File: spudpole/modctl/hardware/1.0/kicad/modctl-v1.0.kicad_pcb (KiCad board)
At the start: 2 copper layers, 75 x 75 mm, 35 parts, among them J1 SWITCH INPUTS ->, J2 OUTPUTS, J3 M12-5PIN, SW1 PRG_SPUD0, SW2 PRG_SPUD1, SW3 INSTANCE, U1 POWER, U10 MCP2551-I-P, U2 POLE0_UP, U3 CNY74-4H, U4 POLE0_DN, U5 POLE1_UP, U6 POLE1_DN, U8 Teensy_3.2, U9 TEC2-2411WI

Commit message: Many tweaks, plus a latex pretty print
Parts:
- added D5: LED_Small, LED_THT:LED_D3.0mm, F.Cu at (51.4, 82.5)
- added R5: 270R, Resistor_THT:R_Axial_DIN0204_L3.6mm_D1.6mm_P5.08mm_Horizontal, F.Cu at (52.7, 87.6)
- J1: value SWITCH INPUTS -> -> SWITCH INPUTS
- J2: value OUTPUTS -> Screw_Terminal_01x10
- renumbered R5 to R6, R6 to R7, R7 to R8, U8 to U7, U9 to U8, U10 to U9
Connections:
- U7 pad 3: (no net) -> Net-(D5-Pad1)
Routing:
- net Net-(D5-Pad1): track 0.00 -> 15.7 mm
- net Net-(D5-Pad2): track 0.00 -> 3.07 mm

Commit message: Utility and config changes
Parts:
- removed the D2 at (-5.71, 68.6)
- added R6: 270R, Resistor_THT:R_Axial_DIN0204_L3.6mm_D1.6mm_P5.08mm_Horizontal, F.Cu at (48.3, 55.2)
- added R7: 270R, Resistor_THT:R_Axial_DIN0204_L3.6mm_D1.6mm_P5.08mm_Horizontal, F.Cu at (48.3, 64.1)
- D1: value 4 x 1N4007 -> 1N4007
- D2: renamed from D5; value LED_Small -> PWR
- D3: value 1N4007 -> UP; footprint Diode_THT:D_DO-35_SOD27_P2.54mm_Vertical_AnodeUp -> LED_THT:LED_D3.0mm
- D4: value 1N4007 -> DN; footprint Diode_THT:D_DO-35_SOD27_P2.54mm_Vertical_AnodeUp -> LED_THT:LED_D3.0mm
- J2: value Screw_Terminal_01x10 -> RELAY OUTPUTS
- R1: value 4 x 1K4, 1W -> 1K4
- R2, R3, R4: value 1K4, 1W -> 1K4
- SW1: value PRG_SPUD0 -> PRGW0
- SW2: value PRG_SPUD1 -> PRGW1
- U1: value POWER -> 291-9669; footprint pdjr:SPNO-SIL -> pdjr:291-9669
- U2: value POLE0_UP -> 291-9669; footprint pdjr:SPNO-SIL -> pdjr:291-9669
- U4: value POLE0_DN -> 291-9669; footprint pdjr:SPNO-SIL -> pdjr:291-9669
- U5: value POLE1_UP -> 291-9669; footprint pdjr:SPNO-SIL -> pdjr:291-9669
- U6: value POLE1_DN -> 291-9669; footprint pdjr:SPNO-SIL -> pdjr:291-9669
- moved D3 57.1 mm to (52.1, 54.0), turned to 270 degrees
- moved D4 48.3 mm to (52.1, 60.3), turned to 270 degrees
- moved D1 26.3 mm to (11.4, 77.5), turned to 90 degrees
- moved C1 16.9 mm to (10.2, 69.2), turned to 180 degrees
- moved D2 15.9 mm to (52.1, 66.7)
- moved R5 15.3 mm to (52.1, 72.4), turned to 270 degrees
- moved SW3 10.3 mm to (34.9, 52.1)
- moved U7 5.71 mm to (23.5, 68.6)
- moved SW1 4.96 mm to (23.5, 45.1), turned to 90 degrees
- moved SW2 4.26 mm to (34.9, 45.1), turned to 90 degrees
- turned U1 to 270 degrees
- turned U2 to 270 degrees
- turned U4 to 270 degrees
- turned U5 to 270 degrees
- turned U6 to 270 degrees
- renumbered R8 to R10, R6 to R8, R7 to R9
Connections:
- D2 pad 1: Net-(D5-Pad1) -> GND
- D2 pad 2: Net-(D5-Pad2) -> Net-(D2-Pad2)
- D3 pad 1: Net-(D3-Pad1) -> GND
- D3 pad 2: Net-(D1-Pad2) -> Net-(D3-Pad2)
- D4 pad 1: Net-(D4-Pad1) -> GND
- D4 pad 2: Net-(D1-Pad2) -> Net-(D4-Pad2)
- J1 pad 5: Net-(D1-Pad2) -> Net-(D1-Pad1)
- R1 pad 2: Net-(D1-Pad1) -> Net-(R1-Pad2)
- R3 pad 2: Net-(D3-Pad1) -> Net-(R3-Pad2)
- R4 pad 2: Net-(D4-Pad1) -> Net-(R4-Pad2)
- R5 pad 1: Net-(D5-Pad2) -> Net-(R5-Pad1)
- R5 pad 2: Net-(C1-Pad1) -> Net-(D2-Pad2)
- SW1 pad 1: Net-(SW1-Pad1) -> GND
- SW1 pad 2: GND -> Net-(SW1-Pad2)
- SW2 pad 1: GND -> Net-(SW2-Pad1)
- SW2 pad 2: Net-(SW2-Pad2) -> GND
- U1 pad 1: Net-(J2-Pad2) -> Net-(J2-Pad1)
- U1 pad 3: GND -> Net-(U1-Pad3)
- U1 pad 5: Net-(U1-Pad5) -> GND
- U1 pad 7: Net-(J2-Pad1) -> Net-(J2-Pad2)
- U2 pad 1: Net-(J2-Pad4) -> Net-(J2-Pad3)
- U2 pad 3: GND -> Net-(U2-Pad3)
- U2 pad 5: Net-(U2-Pad5) -> GND
- U2 pad 7: Net-(J2-Pad3) -> Net-(J2-Pad4)
- U3 pad 1: Net-(D1-Pad1) -> Net-(R1-Pad2)
- U3 pad 5: Net-(D3-Pad1) -> Net-(R3-Pad2)
- U3 pad 8: Net-(D4-Pad1) -> Net-(R4-Pad2)
- U4 pad 1: Net-(J2-Pad6) -> Net-(J2-Pad5)
- U4 pad 3: GND -> Net-(U4-Pad3)
- U4 pad 5: Net-(U4-Pad5) -> GND
- U4 pad 7: Net-(J2-Pad5) -> Net-(J2-Pad6)
- U5 pad 1: Net-(J2-Pad8) -> Net-(J2-Pad7)
- U5 pad 3: GND -> Net-(U5-Pad3)
- U5 pad 5: Net-(U5-Pad5) -> GND
- U5 pad 7: Net-(J2-Pad7) -> Net-(J2-Pad8)
- U6 pad 1: Net-(J2-Pad10) -> Net-(J2-Pad9)
- U6 pad 3: GND -> Net-(U6-Pad3)
- U6 pad 5: Net-(U6-Pad5) -> GND
- U6 pad 7: Net-(J2-Pad9) -> Net-(J2-Pad10)
- U7 pad 19: (no net) -> Net-(U6-Pad3)
- U7 pad 2: Net-(SW2-Pad2) -> Net-(R7-Pad1)
- U7 pad 20: Net-(U6-Pad5) -> Net-(U5-Pad3)
- U7 pad 21: Net-(U5-Pad5) -> Net-(U4-Pad3)
- U7 pad 22: Net-(U4-Pad5) -> Net-(U2-Pad3)
- U7 pad 23: Net-(U2-Pad5) -> Net-(U1-Pad3)
- U7 pad 24: Net-(U1-Pad5) -> Net-(SW1-Pad2)
- U7 pad 25: Net-(SW1-Pad1) -> Net-(SW2-Pad1)
- U7 pad 3: Net-(D5-Pad1) -> Net-(R6-Pad1)
- U7 pad 4: (no net) -> Net-(R5-Pad1)
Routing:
- net Net-(U1-Pad5): track 65.4 -> 0.00 mm
- net Net-(U2-Pad5): track 58.2 -> 0.00 mm
- net Net-(U1-Pad3): track 0.00 -> 58.2 mm
- net Net-(U4-Pad5): track 51.1 -> 0.00 mm
- net Net-(U2-Pad3): track 0.00 -> 51.1 mm
- net Net-(SW2-Pad1): track 0.00 -> 48.8 mm
- net Net-(U5-Pad5): track 44.0 -> 0.00 mm
- net Net-(U4-Pad3): track 0.00 -> 42.8 mm
- net Net-(R6-Pad1): track 0.00 -> 40.1 mm
- net Net-(SW1-Pad2): track 0.00 -> 39.6 mm
- net Net-(U6-Pad5): track 36.8 -> 0.00 mm
- net Net-(SW2-Pad2): track 36.5 -> 0.00 mm
- net Net-(U5-Pad3): track 0.00 -> 35.3 mm
- net Net-(R7-Pad1): track 0.00 -> 32.2 mm
- net Net-(SW1-Pad1): track 31.4 -> 0.00 mm
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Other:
- board text added: "MODCTL"
- board text added: "MODCTL 1.0"
- board text added: "NMEA 2000 Windlass Control Interface Module"
- board text added: "PDJR.EU"
- board text added: "PWR/RX"
- board text added: "SPUD/W0"
- board text added: "SPUD/W1"

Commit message: testing...
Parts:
- R8: footprint Resistor_THT:R_Axial_DIN0204_L3.6mm_D1.6mm_P2.54mm_Vertical -> Resistor_THT:R_Axial_DIN0204_L3.6mm_D1.6mm_P5.08mm_Horizontal
- SW3: footprint Button_Switch_THT:SW_DIP_SPSTx08_Slide_6.7x21.88mm_W7.62mm_P2.54mm_LowProfile -> Package_DIP:DIP-14_W7.62mm_Socket
- U1: value 291-9669 -> POWER
- U2: value 291-9669 -> W0UP
- U4: value 291-9669 -> W0DN
- U5: value 291-9669 -> W1UP
- U6: value 291-9669 -> W1DN
- moved R8 7.24 mm to (19.1, 36.2), turned to 0 degrees
- moved R10 1.91 mm to (19.1, 31.1)
- moved R9 1.91 mm to (24.1, 33.7)
- moved J3 1.27 mm to (29.2, 22.2)
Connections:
- SW3 pad 8: Net-(SW3-Pad8) -> GND
- U7 pad 15: Net-(U3-Pad15) -> (no net)
- U7 pad 16: Net-(U3-Pad14) -> Net-(U3-Pad15)
- U7 pad 17: Net-(U3-Pad11) -> Net-(U3-Pad14)
- U7 pad 18: Net-(U3-Pad10) -> Net-(U3-Pad11)
- U7 pad 19: Net-(U6-Pad3) -> Net-(U3-Pad10)
- U7 pad 2: Net-(R7-Pad1) -> Net-(SW2-Pad1)
- U7 pad 20: Net-(U5-Pad3) -> Net-(U6-Pad3)
- U7 pad 21: Net-(U4-Pad3) -> Net-(U5-Pad3)
- U7 pad 22: Net-(U2-Pad3) -> Net-(U4-Pad3)
- U7 pad 23: Net-(U1-Pad3) -> Net-(U2-Pad3)
- U7 pad 24: Net-(SW1-Pad2) -> Net-(U1-Pad3)
- U7 pad 25: Net-(SW2-Pad1) -> Net-(SW1-Pad2)
- U7 pad 3: Net-(R6-Pad1) -> Net-(R7-Pad1)
- U7 pad 4: Net-(R5-Pad1) -> Net-(R6-Pad1)
- U7 pad 7: Net-(SW3-Pad8) -> Net-(R5-Pad1)
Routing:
- net Net-(R7-Pad1): track 32.2 -> 69.0 mm
- net Net-(R8-Pad2): track 17.5 -> 3.18 mm
- net Net-(R6-Pad1): track 40.1 -> 51.3 mm
- net Net-(U1-Pad3): track 58.2 -> 64.1 mm
- net Net-(U5-Pad3): track 35.3 -> 41.0 mm
- net Net-(U4-Pad3): track 42.8 -> 47.8 mm
- net Net-(U2-Pad3): track 51.1 -> 55.7 mm
- net Net-(C3-Pad1): track 13.2 -> 17.5 mm
- net Net-(SW3-Pad8): track 3.81 -> 0.00 mm
- net Net-(R5-Pad1): track 25.3 -> 22.0 mm
- net Net-(SW2-Pad1): track 48.8 -> 45.7 mm
- net Net-(U6-Pad3): track 29.3 -> 32.0 mm
- net Net-(SW1-Pad2): track 39.6 -> 42.1 mm
- net Net-(U3-Pad10): track 16.4 -> 18.7 mm
- net Net-(J3-Pad4): track 22.8 -> 20.8 mm
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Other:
- board text removed: "128"

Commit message: Refactor
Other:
- board text added: "W0"
- board text added: "W1"
- board text removed: "SPUD/W0"
- board text removed: "SPUD/W1"

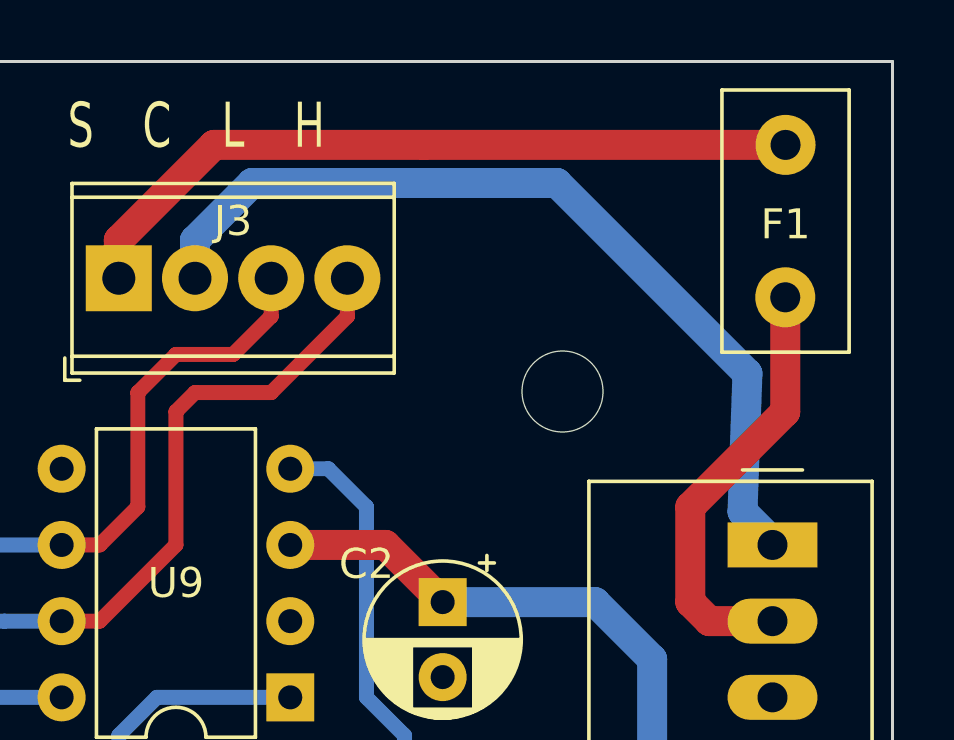
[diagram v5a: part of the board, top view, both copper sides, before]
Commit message: Grounded NMEA C connection
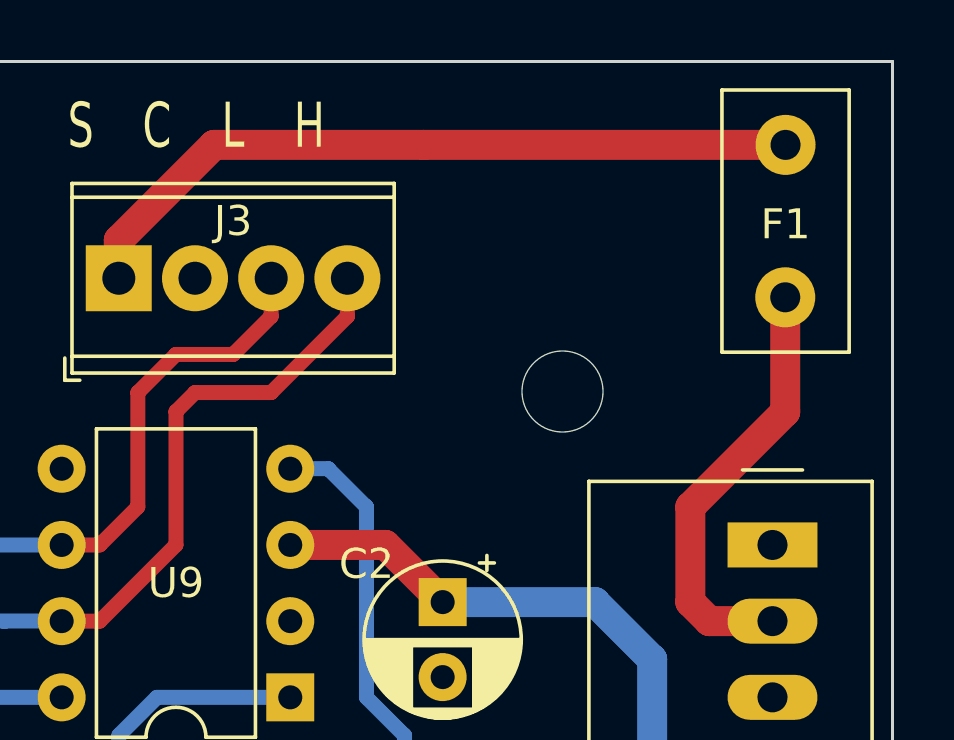
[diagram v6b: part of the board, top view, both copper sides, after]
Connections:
- J3 pad 2: Net-(J3-Pad2) -> GND
- U8 pad 1: Net-(J3-Pad2) -> GND
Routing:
- net Net-(J3-Pad2): track 29.2 -> 0.00 mm

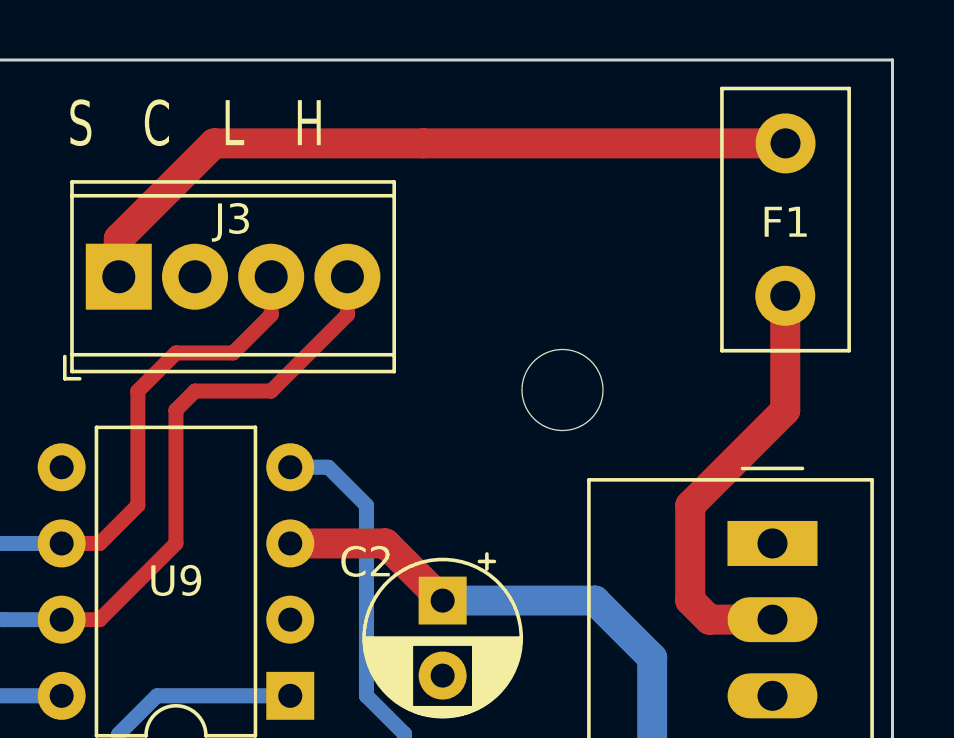
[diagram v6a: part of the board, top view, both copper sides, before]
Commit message: New print script
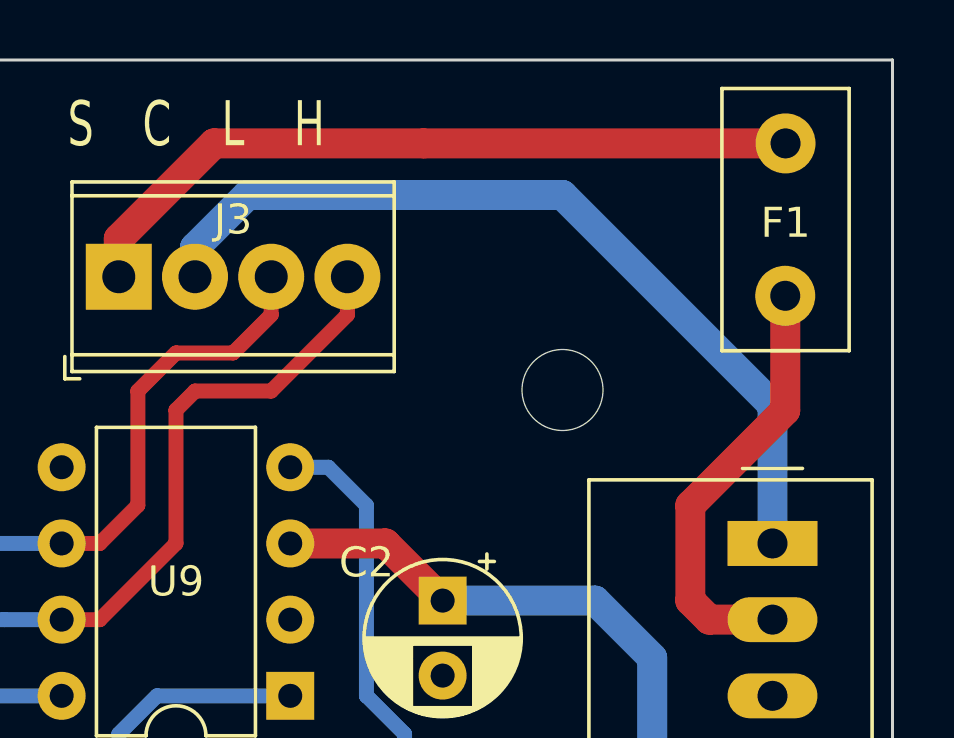
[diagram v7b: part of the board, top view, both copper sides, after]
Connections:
- J3 pad 2: GND -> Net-(J3-Pad2)
- U8 pad 1: GND -> Net-(J3-Pad2)
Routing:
- net Net-(J3-Pad2): track 0.00 -> 28.5 mm
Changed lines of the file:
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@@
     (thickness 1.6)
     (drawings 181)
-    (tracks 302)
+    (tracks 307)
     (zones 0)
     (modules 38)
-    (nets 56)
+    (nets 57)
   )
   (page A4)
@@
     (39 F.Mask user hide)
     (40 Dwgs.User user hide)
-    (41 Cmts.User user hide)
+    (41 Cmts.User user)
     (42 Eco1.User user hide)
     (43 Eco2.User user hide)
@@
   )
   (setup
-    (last_trace_width 0.25)
+    (last_trace_width 1)
     (user_trace_width 0.5)
     (user_trace_width 1)
@@
   (net 54 "Net-(R3-Pad2)")
   (net 55 "Net-(R4-Pad2)")
+  (net 56 "Net-(J3-Pad2)")
   (net_class Default "This is the default net class."
     (clearance 0.2)
@@
     (add_net "Net-(J2-Pad8)")
     (add_net "Net-(J2-Pad9)")
+    (add_net "Net-(J3-Pad2)")
     (add_net "Net-(J3-Pad3)")
     (add_net "Net-(J3-Pad4)")
@@
       (net 7 "Net-(F1-Pad2)"))
     (pad 1 thru_hole rect (at 0 0 270) (size 1.5 3) (drill 1) (layers *.Cu *.Mask)
-      (net 1 GND))
+      (net 56 "Net-(J3-Pad2)"))
     (model ${KISYS3DMOD}/Converter_DCDC.3dshapes/Converter_DCDC_TRACO_TMR-xxxx_THT.wrl
       (at (xyz 0 0 0))
@@
       (net 24 "Net-(J3-Pad3)"))
     (pad 2 thru_hole circle (at 2.54 0) (size 2.2 2.2) (drill 1.1) (layers *.Cu *.Mask)
-      (net 1 GND))
+      (net 56 "Net-(J3-Pad2)"))
     (pad 1 thru_hole rect (at 0 0) (size 2.2 2.2) (drill 1.1) (layers *.Cu *.Mask)
       (net 8 "Net-(F1-Pad1)"))
@@
   (segment (start 8.255 74.295) (end 4.445 70.485) (width 0.5) (layer B.Cu) (net 55))
   (segment (start 8.255 74.93) (end 8.255 74.295) (width 0.5) (layer B.Cu) (net 55))
+  (segment (start 44 19.5) (end 51 26.5) (width 1) (layer B.Cu) (net 56))
+  (segment (start 33.5 19.5) (end 44 19.5) (width 1) (layer B.Cu) (net 56))
+  (segment (start 31.75 22.225) (end 31.75 21.25) (width 1) (layer B.Cu) (net 56))
+  (segment (start 51 26.5) (end 51 31.115) (width 1) (layer B.Cu) (net 56))
+  (segment (start 31.75 21.25) (end 33.5 19.5) (width 1) (layer B.Cu) (net 56))
   (zone (net 1) (net_name GND) (layer F.Cu) (hatch edge 0.508)
     (connect_pads (clearance 0.508))

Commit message: New PCB layout
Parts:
- added JP1: Jumper_2_Open, Connector_PinHeader_2.54mm:PinHeader_1x02_P2.54mm_Vertical, F.Cu at (-10.2, 53.3)
- added JP2: Jumper_2_Open, Connector_PinHeader_2.54mm:PinHeader_1x02_P2.54mm_Vertical, F.Cu at (-4.45, 53.3)
- added JP3: Jumper_2_Open, Connector_PinHeader_2.54mm:PinHeader_1x02_P2.54mm_Vertical, F.Cu at (1.27, 53.3)
- added JP4: Jumper_2_Open, Connector_PinHeader_2.54mm:PinHeader_1x02_P2.54mm_Vertical, F.Cu at (6.99, 53.3)
- moved U3 6.36 mm to (-13.3, 70.5)
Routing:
- net Net-(J2-Pad2): track 43.9 -> 73.3 mm
- net Net-(D1-Pad2): track 35.9 -> 28.2 mm
- net Net-(R4-Pad2): track 12.4 -> 6.02 mm
- net Net-(R2-Pad2): track 16.2 -> 10.6 mm
- net Net-(R1-Pad2): track 20.3 -> 14.6 mm
- net Net-(J2-Pad8): track 36.2 -> 41.3 mm
- net Net-(J2-Pad6): track 37.2 -> 42.3 mm
- net Net-(J2-Pad4): track 37.8 -> 42.9 mm
- net Net-(J2-Pad10): track 33.7 -> 38.8 mm
- net Net-(R3-Pad2): track 16.1 -> 11.6 mm
- net Net-(U3-Pad11): track 21.2 -> 18.6 mm
- net Net-(U2-Pad3): track 55.7 -> 53.8 mm
- net Net-(U3-Pad10): track 18.7 -> 17.1 mm
- net Net-(U3-Pad14): track 28.8 -> 27.3 mm
- net Net-(U4-Pad3): track 47.8 -> 46.7 mm
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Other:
- board text added: "WCTL"
- board text added: "WCTL 1.0"
- board text removed: "MODCTL"
- board text removed: "MODCTL 1.0"
